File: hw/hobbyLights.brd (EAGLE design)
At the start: 50 x 35 mm, 56 parts, among them U1 MCP73831-2, U2 POWER, U3 BD48K28G, U4 ATMEGA32U4-AU, U5 TPS61222, Y1 RESONATORSMD

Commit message: Minor reviews on the PCB
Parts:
- moved R11 0.86 mm to (22.2, 18.9), turned to 90 degrees
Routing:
- removed copper zone on layer 16, net DGND
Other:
- board text removed: "electroFUN microDriver"
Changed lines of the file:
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@@
 <?xml version="1.0" encoding="utf-8"?>
 <!DOCTYPE eagle SYSTEM "eagle.dtd">
-<eagle version="7.0.0">
+<eagle version="7.5.0">
 <drawing>
 <settings>
@@
 <board>
 <plain>
-<text x="6.096" y="25.019" size="1.27" layer="22" font="vector" ratio="16" rot="MR0">Vbat</text>
+<text x="5.1435" y="25.2095" size="1.27" layer="22" font="vector" ratio="16" rot="MR0">Vbat</text>
 <wire x1="0" y1="32.64770625" x2="0" y2="2.83980625" width="0.254" layer="20"/>
 <wire x1="0" y1="2.83980625" x2="2.83980625" y2="0" width="0.254" layer="20" curve="90"/>
@@
 <text x="10.922" y="5.842" size="1.016" layer="21" font="vector" ratio="15" rot="R90">CHRG.</text>
 <wire x1="2.2225" y1="34.9885" x2="47.498" y2="34.9885" width="0.254" layer="20"/>
-<text x="20.447" y="40.767" size="1.27" layer="26" ratio="12" rot="MR0">electroFUN
-microDriver</text>
-<text x="40.64" y="40.894" size="1.27" layer="26" ratio="12" rot="MR0">electroFUN
-microDriver</text>
 </plain>
 <attributes>
@@
 <attribute name="VALUE" x="35.3695" y="12.573" size="0.4064" layer="27" rot="R270"/>
 </element>
-<element name="R11" library="rcl" package="R0603" value="10k" x="21.717" y="18.161" smashed="yes" rot="R180">
-<attribute name="NAME" x="22.606" y="20.193" size="0.8128" layer="25" ratio="12" rot="R180"/>
-<attribute name="VALUE" x="23.622" y="20.066" size="0.8128" layer="27" ratio="12" rot="R180"/>
+<element name="R11" library="rcl" package="R0603" value="10k" x="22.225" y="18.8595" smashed="yes" rot="R90">
+<attribute name="NAME" x="23.495" y="21.463" size="0.8128" layer="25" ratio="12" rot="R180"/>
+<attribute name="VALUE" x="24.13" y="16.9545" size="0.8128" layer="27" ratio="12" rot="R90"/>
 </element>
 <element name="C8" library="rcl" package="C0603" value="0.1nF" x="36.703" y="8.001" smashed="yes" rot="R270">
@@
 <via x="8.382" y="13.843" extent="1-16" drill="0.3"/>
 <contactref element="U$4" pad="GND"/>
-<via x="31.496" y="1.905" extent="1-16" drill="0.3"/>
+<via x="31.369" y="1.905" extent="1-16" drill="0.3"/>
 <via x="31.369" y="4.191" extent="1-16" drill="0.3"/>
 <contactref element="C13" pad="2"/>
@@
 <contactref element="C12" pad="2"/>
 <contactref element="C16" pad="2"/>
-<via x="21.717" y="17.145" extent="1-16" drill="0.3"/>
+<via x="21.1455" y="17.018" extent="1-16" drill="0.3"/>
 <via x="20.701" y="15.367" extent="1-16" drill="0.3"/>
 <via x="20.3835" y="13.462" extent="1-16" drill="0.3"/>
@@
 <via x="47.498" y="2.921" extent="1-16" drill="0.3"/>
 <via x="27.559" y="4.953" extent="1-16" drill="0.3"/>
-<via x="24.13" y="21.59" extent="1-16" drill="0.3"/>
-<via x="24.13" y="20.32" extent="1-16" drill="0.3"/>
-<via x="21.59" y="20.32" extent="1-16" drill="0.3"/>
+<via x="22.86" y="21.59" extent="1-16" drill="0.3"/>
+<via x="23.495" y="20.5105" extent="1-16" drill="0.3"/>
+<via x="20.955" y="20.5105" extent="1-16" drill="0.3"/>
 <via x="12.192" y="13.97" extent="1-16" drill="0.3"/>
 <via x="8.636" y="23.114" extent="1-16" drill="0.3"/>
@@
 <wire x1="26.797" y1="23.241" x2="26.797" y2="22.987" width="0.3048" layer="1"/>
 <wire x1="26.797" y1="22.987" x2="26.924" y2="22.86" width="0.3048" layer="1"/>
-<wire x1="26.797" y1="23.241" x2="27.051" y2="22.86" width="0.3048" layer="1"/>
+<wire x1="26.797" y1="23.241" x2="27.178" y2="22.86" width="0.3048" layer="1"/>
 <wire x1="26.797" y1="23.241" x2="26.416" y2="22.86" width="0.3048" layer="1"/>
 <wire x1="19.939" y1="22.479" x2="19.558" y2="22.86" width="0.3048" layer="1"/>
@@
 <wire x1="38.735" y1="8.255" x2="38.735" y2="6.135" width="0.3556" layer="1"/>
 <wire x1="38.735" y1="6.135" x2="36.918" y2="4.318" width="0.3556" layer="1"/>
-<wire x1="27.051" y1="22.86" x2="34.163" y2="22.86" width="0.3048" layer="1"/>
+<wire x1="27.178" y1="22.86" x2="34.163" y2="22.86" width="0.3048" layer="1"/>
 <wire x1="34.163" y1="22.86" x2="34.671" y2="23.368" width="0.3048" layer="1"/>
 <wire x1="34.671" y1="23.368" x2="34.671" y2="26.924" width="0.3048" layer="1"/>
@@
 <wire x1="28.867" y1="8.039" x2="28.7655" y2="7.9375" width="0.254" layer="1"/>
 <wire x1="17.206" y1="13.335" x2="17.206" y2="11.242" width="0.3556" layer="1"/>
-<wire x1="27.051" y1="22.86" x2="26.924" y2="22.86" width="0.3048" layer="1"/>
+<wire x1="27.178" y1="22.86" x2="26.924" y2="22.86" width="0.3048" layer="1"/>
 <wire x1="20.32" y1="22.86" x2="19.939" y2="22.479" width="0.3048" layer="1"/>
 <wire x1="28.868" y1="3.048" x2="28.868" y2="6.391" width="0.3048" layer="1"/>
@@
 <contactref element="U4" pad="33"/>
 <contactref element="R11" pad="1"/>
-<wire x1="24.067" y1="17.992" x2="23.664" y2="17.992" width="0.3048" layer="1"/>
-<wire x1="23.664" y1="17.992" x2="23.495" y2="18.161" width="0.3048" layer="1"/>
-<wire x1="23.495" y1="18.161" x2="22.567" y2="18.161" width="0.3048" layer="1"/>
+<wire x1="24.067" y1="17.992" x2="22.225" y2="17.992" width="0.3048" layer="1"/>
+<wire x1="22.225" y1="17.992" x2="22.225" y2="18.0095" width="0.4064" layer="1"/>
 </signal>
 <signal name="D13">
@@
 <signal name="N$8">
 </signal>
-<signal name="DGND">
-<polygon width="0.254" layer="16">
-<vertex x="6.604" y="46.228"/>
-<vertex x="23.495" y="46.228"/>
-<vertex x="23.495" y="38.227"/>
-<vertex x="6.604" y="38.227"/>
-</polygon>
-<polygon width="0.254" layer="16">
-<vertex x="27.305" y="46.228"/>
-<vertex x="27.305" y="38.227"/>
-<vertex x="43.815" y="38.227"/>
-<vertex x="43.815" y="46.355"/>
-<vertex x="27.305" y="46.355"/>
-</polygon>
-</signal>
 </signals>
 <errors>
@@
 </board>
 </drawing>
-<compatibility>
-<note version="6.3" minversion="6.2.2" severity="warning">
-Since Version 6.2.2 text objects can contain more than one line,
-which will not be processed correctly with this version.
-</note>
-</compatibility>
 </eagle>

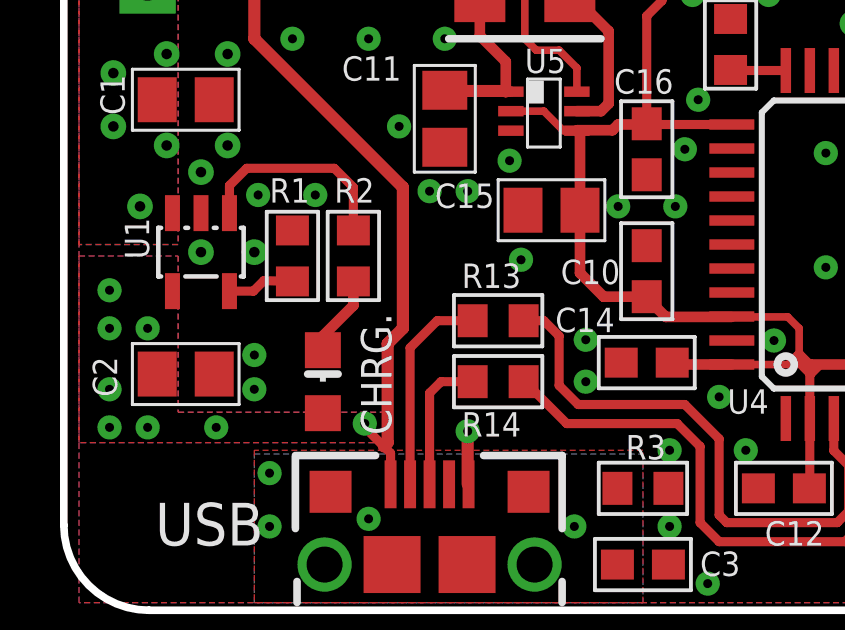
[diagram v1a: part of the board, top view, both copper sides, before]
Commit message: Updated PCB removing daughter motor boards.
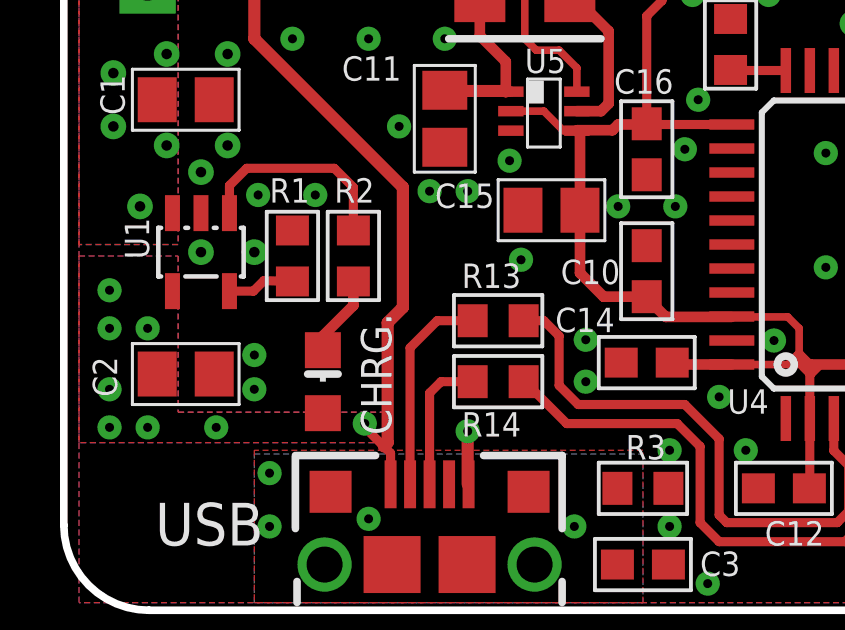
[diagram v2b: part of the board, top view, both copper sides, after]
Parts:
- C10, C13, C14, C16, C5, C6, C7, C8, C9: value 0.1nF -> 0.1uF
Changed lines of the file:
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@@
 <?xml version="1.0" encoding="utf-8"?>
 <!DOCTYPE eagle SYSTEM "eagle.dtd">
-<eagle version="7.5.0">
+<eagle version="7.4.0">
 <drawing>
 <settings>
@@
 <layers>
 <layer number="1" name="Top" color="4" fill="1" visible="yes" active="yes"/>
-<layer number="16" name="Bottom" color="1" fill="1" visible="no" active="yes"/>
+<layer number="16" name="Bottom" color="1" fill="1" visible="yes" active="yes"/>
 <layer number="17" name="Pads" color="2" fill="1" visible="yes" active="yes"/>
 <layer number="18" name="Vias" color="2" fill="1" visible="yes" active="yes"/>
@@
 <attribute name="VALUE" x="37.973" y="21.463" size="0.8128" layer="27" ratio="12"/>
 </element>
-<element name="C5" library="rcl" package="C0603" value="0.1nF" x="20.32" y="24.765" smashed="yes" rot="R90">
+<element name="C5" library="rcl" package="C0603" value="0.1uF" x="20.32" y="24.765" smashed="yes" rot="R90">
 <attribute name="NAME" x="21.082" y="22.987" size="0.8128" layer="25" ratio="12" rot="R180"/>
 <attribute name="VALUE" x="22.86" y="23.495" size="0.8128" layer="27" ratio="12" rot="R90"/>
 </element>
-<element name="C6" library="rcl" package="C0603" value="0.1nF" x="28.702" y="24.765" smashed="yes" rot="R90">
+<element name="C6" library="rcl" package="C0603" value="0.1uF" x="28.702" y="24.765" smashed="yes" rot="R90">
 <attribute name="NAME" x="29.591" y="22.987" size="0.8128" layer="25" ratio="12" rot="R180"/>
 <attribute name="VALUE" x="31.242" y="23.495" size="0.8128" layer="27" ratio="12" rot="R90"/>
 </element>
-<element name="C7" library="rcl" package="C0603" value="0.1nF" x="36.322" y="24.765" smashed="yes" rot="R90">
+<element name="C7" library="rcl" package="C0603" value="0.1uF" x="36.322" y="24.765" smashed="yes" rot="R90">
 <attribute name="NAME" x="36.83" y="22.987" size="0.8128" layer="25" ratio="12" rot="R180"/>
 <attribute name="VALUE" x="38.862" y="23.495" size="0.8128" layer="27" ratio="12" rot="R90"/>
@@
 <attribute name="VALUE" x="24.13" y="16.9545" size="0.8128" layer="27" ratio="12" rot="R90"/>
 </element>
-<element name="C8" library="rcl" package="C0603" value="0.1nF" x="36.703" y="8.001" smashed="yes" rot="R270">
+<element name="C8" library="rcl" package="C0603" value="0.1uF" x="36.703" y="8.001" smashed="yes" rot="R270">
 <attribute name="NAME" x="37.719" y="7.366" size="0.8128" layer="25" ratio="12"/>
 <attribute name="VALUE" x="34.671" y="10.287" size="0.8128" layer="27" ratio="12" rot="R270"/>
 </element>
-<element name="C9" library="rcl" package="C0603" value="0.1nF" x="29.718" y="3.048" smashed="yes">
+<element name="C9" library="rcl" package="C0603" value="0.1uF" x="29.718" y="3.048" smashed="yes">
 <attribute name="NAME" x="29.718" y="1.905" size="0.8128" layer="25" ratio="12" rot="R180"/>
 <attribute name="VALUE" x="27.432" y="1.016" size="0.8128" layer="27" ratio="12"/>
 </element>
-<element name="C10" library="rcl" package="C0603" value="0.1nF" x="19.431" y="11.303" smashed="yes" rot="R90">
+<element name="C10" library="rcl" package="C0603" value="0.1uF" x="19.431" y="11.303" smashed="yes" rot="R90">
 <attribute name="NAME" x="18.542" y="11.684" size="0.8128" layer="25" ratio="12" rot="R180"/>
 <attribute name="VALUE" x="21.463" y="9.017" size="0.8128" layer="27" ratio="12" rot="R90"/>
@@
 <element name="U$6" library="fmc" package="BOARD_REF" value="" x="43.18" y="6.35" rot="MR0"/>
 <element name="U$7" library="fmc" package="GEEKKIDS_S" value="" x="43.18" y="24.003" rot="MR0"/>
-<element name="C13" library="rcl" package="C0603" value="0.1nF" x="34.544" y="19.177"/>
-<element name="C14" library="rcl" package="C0603" value="0.1nF" x="19.431" y="8.255" smashed="yes" rot="R180">
+<element name="C13" library="rcl" package="C0603" value="0.1uF" x="34.544" y="19.177"/>
+<element name="C14" library="rcl" package="C0603" value="0.1uF" x="19.431" y="8.255" smashed="yes" rot="R180">
 <attribute name="NAME" x="16.383" y="9.271" size="0.8128" layer="25" ratio="12"/>
 <attribute name="VALUE" x="21.717" y="10.287" size="0.8128" layer="27" ratio="12" rot="R180"/>
@@
 <attribute name="VALUE" x="38.227" y="21.717" size="1.27" layer="27" rot="R270"/>
 </element>
-<element name="C16" library="rcl" package="C0603" value="0.1nF" x="19.431" y="15.367" smashed="yes" rot="R270">
+<element name="C16" library="rcl" package="C0603" value="0.1uF" x="19.431" y="15.367" smashed="yes" rot="R270">
 <attribute name="NAME" x="20.32" y="18.034" size="0.8128" layer="25" ratio="12" rot="R180"/>
 <attribute name="VALUE" x="17.399" y="17.653" size="0.8128" layer="27" ratio="12" rot="R270"/>
@@
 <wire x1="10.892" y1="5.237" x2="10.668" y2="5.461" width="0.3048" layer="1"/>
 <wire x1="10.668" y1="5.461" x2="10.16" y2="5.969" width="0.3048" layer="1"/>
-<wire x1="11.303" y1="14.097" x2="11.303" y2="9.398" width="0.4064" layer="1"/>
-<wire x1="11.303" y1="9.398" x2="10.795" y2="8.89" width="0.4064" layer="1"/>
-<wire x1="10.795" y1="8.89" x2="10.795" y2="5.588" width="0.4064" layer="1"/>
+<wire x1="11.303" y1="14.097" x2="11.303" y2="10.0965" width="0.4064" layer="1"/>
+<wire x1="11.303" y1="10.0965" x2="10.795" y2="9.5885" width="0.4064" layer="1"/>
+<wire x1="10.795" y1="9.5885" x2="10.795" y2="5.588" width="0.4064" layer="1"/>
 <wire x1="10.795" y1="5.588" x2="10.668" y2="5.461" width="0.4064" layer="1"/>
 <contactref element="U2" pad="P4"/>

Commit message: Initial program configuration.
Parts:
- moved C14 0.13 mm to (19.3, 8.26)
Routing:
- net GND: vias 97 -> 99
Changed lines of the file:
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@@
 <element name="U$7" library="fmc" package="GEEKKIDS_S" value="" x="43.18" y="24.003" rot="MR0"/>
 <element name="C13" library="rcl" package="C0603" value="0.1uF" x="34.544" y="19.177"/>
-<element name="C14" library="rcl" package="C0603" value="0.1uF" x="19.431" y="8.255" smashed="yes" rot="R180">
-<attribute name="NAME" x="16.383" y="9.271" size="0.8128" layer="25" ratio="12"/>
-<attribute name="VALUE" x="21.717" y="10.287" size="0.8128" layer="27" ratio="12" rot="R180"/>
+<element name="C14" library="rcl" package="C0603" value="0.1uF" x="19.304" y="8.255" smashed="yes" rot="R180">
+<attribute name="NAME" x="16.256" y="9.271" size="0.8128" layer="25" ratio="12"/>
+<attribute name="VALUE" x="21.59" y="10.287" size="0.8128" layer="27" ratio="12" rot="R180"/>
 </element>
 <element name="U5" library="fmc" package="DCK" value="TPS61222" x="16.002" y="16.637" smashed="yes" rot="R270">
@@
 <vertex x="50.8" y="0.254"/>
 </polygon>
-<via x="4.572" y="11.938" extent="1-16" drill="0.35"/>
-<via x="6.35" y="11.938" extent="1-16" drill="0.35"/>
-<via x="5.461" y="15.494" extent="1-16" drill="0.35"/>
-<via x="5.461" y="18.542" extent="1-16" drill="0.35"/>
-<via x="4.572" y="14.605" extent="1-16" drill="0.35"/>
+<via x="4.572" y="11.938" extent="1-16" drill="0.3"/>
+<via x="6.35" y="11.938" extent="1-16" drill="0.3"/>
+<via x="5.461" y="15.494" extent="1-16" drill="0.3"/>
+<via x="5.461" y="18.542" extent="1-16" drill="0.3"/>
+<via x="4.572" y="14.605" extent="1-16" drill="0.3"/>
 <via x="6.35" y="7.366" extent="1-16" drill="0.3"/>
 <via x="6.477" y="13.843" extent="1-16" drill="0.3"/>
@@
 <via x="20.3835" y="13.462" extent="1-16" drill="0.3"/>
 <via x="18.4785" y="13.462" extent="1-16" drill="0.3"/>
-<via x="17.399" y="9.017" extent="1-16" drill="0.3"/>
-<via x="17.399" y="7.62" extent="1-16" drill="0.3"/>
+<via x="17.272" y="9.017" extent="1-16" drill="0.3"/>
+<via x="17.272" y="7.874" extent="1-16" drill="0.3"/>
 <via x="38.2905" y="10.9855" extent="1-16" drill="0.3"/>
 <via x="25.4" y="15.24" extent="1-16" drill="0.3"/>
@@
 <via x="13.462" y="13.97" extent="1-16" drill="0.3"/>
 <via x="9.906" y="23.114" extent="1-16" drill="0.3"/>
-<via x="14.859" y="14.986" extent="1-16" drill="0.3"/>
+<via x="14.351" y="14.986" extent="1-16" drill="0.3"/>
 <via x="32.258" y="10.668" extent="1-16" drill="0.3"/>
 <via x="33.02" y="17.907" extent="1-16" drill="0.3"/>
@@
 <via x="16.637" y="30.099" extent="1-16" drill="0.3"/>
 <via x="14.351" y="30.099" extent="1-16" drill="0.3"/>
-<via x="16.637" y="23.749" extent="1-16" drill="0.3"/>
+<via x="16.51" y="23.368" extent="1-16" drill="0.3"/>
 <via x="18.669" y="21.59" extent="1-16" drill="0.3"/>
 <via x="13.97" y="23.368" extent="1-16" drill="0.3"/>
-<via x="11.43" y="22.86" extent="1-16" drill="0.3"/>
+<via x="11.43" y="23.114" extent="1-16" drill="0.3"/>
+<via x="15.4305" y="14.986" extent="1-16" drill="0.3"/>
+<via x="16.383" y="14.986" extent="1-16" drill="0.3"/>
 </signal>
 <signal name="N$4">
@@
 <wire x1="11.237" y1="24.219" x2="12.496" y2="24.219" width="0.4064" layer="1"/>
 <wire x1="12.496" y1="24.219" x2="13.208" y2="24.931" width="0.4064" layer="1"/>
-<wire x1="15.367" y1="19.05" x2="15.367" y2="24.003" width="0.254" layer="1"/>
-<wire x1="15.367" y1="24.003" x2="15.494" y2="24.13" width="0.254" layer="1"/>
-<wire x1="15.494" y1="24.13" x2="15.494" y2="24.931" width="0.254" layer="1"/>
+<wire x1="15.367" y1="19.05" x2="15.367" y2="22.733" width="0.254" layer="1"/>
+<wire x1="15.367" y1="22.733" x2="15.494" y2="22.86" width="0.254" layer="1"/>
+<wire x1="15.494" y1="22.86" x2="15.494" y2="24.931" width="0.254" layer="1"/>
 </signal>
 <signal name="N$2">
@@
 <via x="30.48" y="4.953" extent="1-16" drill="0.3"/>
 <wire x1="30.48" y1="4.953" x2="30.734" y2="5.207" width="0.254" layer="16"/>
-<wire x1="30.734" y1="5.207" x2="33.528" y2="5.207" width="0.254" layer="16"/>
-<wire x1="33.528" y1="5.207" x2="35.56" y2="3.175" width="0.254" layer="16"/>
-<wire x1="35.56" y1="3.175" x2="44.196" y2="3.175" width="0.254" layer="16"/>
+<wire x1="30.734" y1="5.207" x2="33.7185" y2="5.207" width="0.254" layer="16"/>
+<wire x1="33.7185" y1="5.207" x2="35.7505" y2="3.175" width="0.254" layer="16"/>
+<wire x1="35.7505" y1="3.175" x2="44.196" y2="3.175" width="0.254" layer="16"/>
 <wire x1="44.196" y1="3.175" x2="44.45" y2="2.921" width="0.254" layer="16"/>
 <wire x1="44.45" y1="2.921" x2="44.45" y2="1.381" width="0.254" layer="16"/>
@@
 <wire x1="24.13" y1="9.779" x2="22.254" y2="9.779" width="0.254" layer="1"/>
 <wire x1="22.267" y1="8.192" x2="20.344" y2="8.192" width="0.3556" layer="1"/>
-<wire x1="20.344" y1="8.192" x2="20.281" y2="8.255" width="0.3048" layer="1"/>
+<wire x1="20.344" y1="8.192" x2="20.154" y2="8.255" width="0.3048" layer="1"/>
 <wire x1="14.902" y1="16.637" x2="16.002" y2="16.637" width="0.254" layer="1"/>
 <wire x1="16.002" y1="16.637" x2="16.652" y2="15.987" width="0.254" layer="1"/>
@@
 <wire x1="26.467" y1="17.992" x2="26.467" y2="19.38" width="0.3048" layer="1"/>
 <wire x1="26.467" y1="19.38" x2="26.289" y2="19.558" width="0.3048" layer="1"/>
-<via x="26.289" y="19.558" extent="1-16" drill="0.35"/>
+<via x="26.289" y="19.558" extent="1-16" drill="0.3"/>
 <wire x1="26.289" y1="19.558" x2="26.289" y2="24.511" width="0.3048" layer="16"/>
 <wire x1="26.289" y1="24.511" x2="22.86" y2="28.067" width="0.3048" layer="16"/>
-<via x="22.86" y="28.067" extent="1-16" drill="0.35"/>
+<via x="22.86" y="28.067" extent="1-16" drill="0.3"/>
 <wire x1="22.86" y1="28.067" x2="22.86" y2="28.829" width="0.3048" layer="1"/>
 <wire x1="22.86" y1="28.829" x2="23.622" y2="29.591" width="0.3048" layer="1"/>
@@
 <wire x1="27.267" y1="17.992" x2="27.267" y2="20.485" width="0.3048" layer="1"/>
 <wire x1="27.267" y1="20.485" x2="27.178" y2="20.574" width="0.3048" layer="1"/>
-<via x="27.178" y="20.574" extent="1-16" drill="0.35"/>
+<via x="27.178" y="20.574" extent="1-16" drill="0.3"/>
 <wire x1="27.178" y1="20.574" x2="27.178" y2="26.289" width="0.3048" layer="16"/>
 <wire x1="27.178" y1="26.289" x2="25.781" y2="27.686" width="0.3048" layer="16"/>
 <wire x1="25.781" y1="27.686" x2="25.781" y2="28.067" width="0.3048" layer="16"/>
-<via x="25.781" y="28.067" extent="1-16" drill="0.35"/>
+<via x="25.781" y="28.067" extent="1-16" drill="0.3"/>
 <wire x1="25.781" y1="28.067" x2="25.781" y2="28.448" width="0.3048" layer="1"/>
 <wire x1="25.781" y1="28.448" x2="26.797" y2="29.464" width="0.3048" layer="1"/>
@@
 <wire x1="34.29" y1="28.829" x2="34.29" y2="28.448" width="0.3048" layer="1"/>
 <wire x1="34.29" y1="28.448" x2="34.163" y2="28.321" width="0.3048" layer="1"/>
-<via x="34.163" y="28.321" extent="1-16" drill="0.35"/>
+<via x="34.163" y="28.321" extent="1-16" drill="0.3"/>
 <wire x1="34.163" y1="28.321" x2="29.972" y2="28.321" width="0.3048" layer="16"/>
 <wire x1="29.972" y1="28.321" x2="28.067" y2="26.416" width="0.3048" layer="16"/>
 <wire x1="28.067" y1="26.416" x2="28.067" y2="21.59" width="0.3048" layer="16"/>
-<via x="28.067" y="21.59" extent="1-16" drill="0.35"/>
+<via x="28.067" y="21.59" extent="1-16" drill="0.3"/>
 <wire x1="28.067" y1="21.59" x2="28.067" y2="17.992" width="0.3048" layer="1"/>
 <wire x1="40.093" y1="24.003" x2="40.093" y2="26.035" width="0.3048" layer="1"/>
@@
 <vertex x="3.81" y="12.192"/>
 </polygon>
-<via x="2.54" y="13.462" extent="1-16" drill="0.35"/>
-<via x="1.651" y="16.129" extent="1-16" drill="0.35"/>
-<via x="1.651" y="17.907" extent="1-16" drill="0.35"/>
-<via x="3.429" y="15.494" extent="1-16" drill="0.35"/>
-<via x="3.429" y="18.542" extent="1-16" drill="0.35"/>
+<via x="2.54" y="13.462" extent="1-16" drill="0.3"/>
+<via x="1.651" y="16.129" extent="1-16" drill="0.3"/>
+<via x="1.651" y="17.907" extent="1-16" drill="0.3"/>
+<via x="3.429" y="15.494" extent="1-16" drill="0.3"/>
+<via x="3.429" y="18.542" extent="1-16" drill="0.3"/>
 <wire x1="2.794" y1="20.828" x2="4.445" y2="20.828" width="0.4064" layer="1"/>
 <wire x1="4.445" y1="20.828" x2="5.08" y2="21.463" width="0.4064" layer="1"/>
